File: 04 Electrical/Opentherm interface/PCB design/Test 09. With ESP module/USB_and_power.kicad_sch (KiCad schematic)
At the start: 18 parts, among them J1 USB-C port, U2 SGM2212-3.3XKC3G/TR

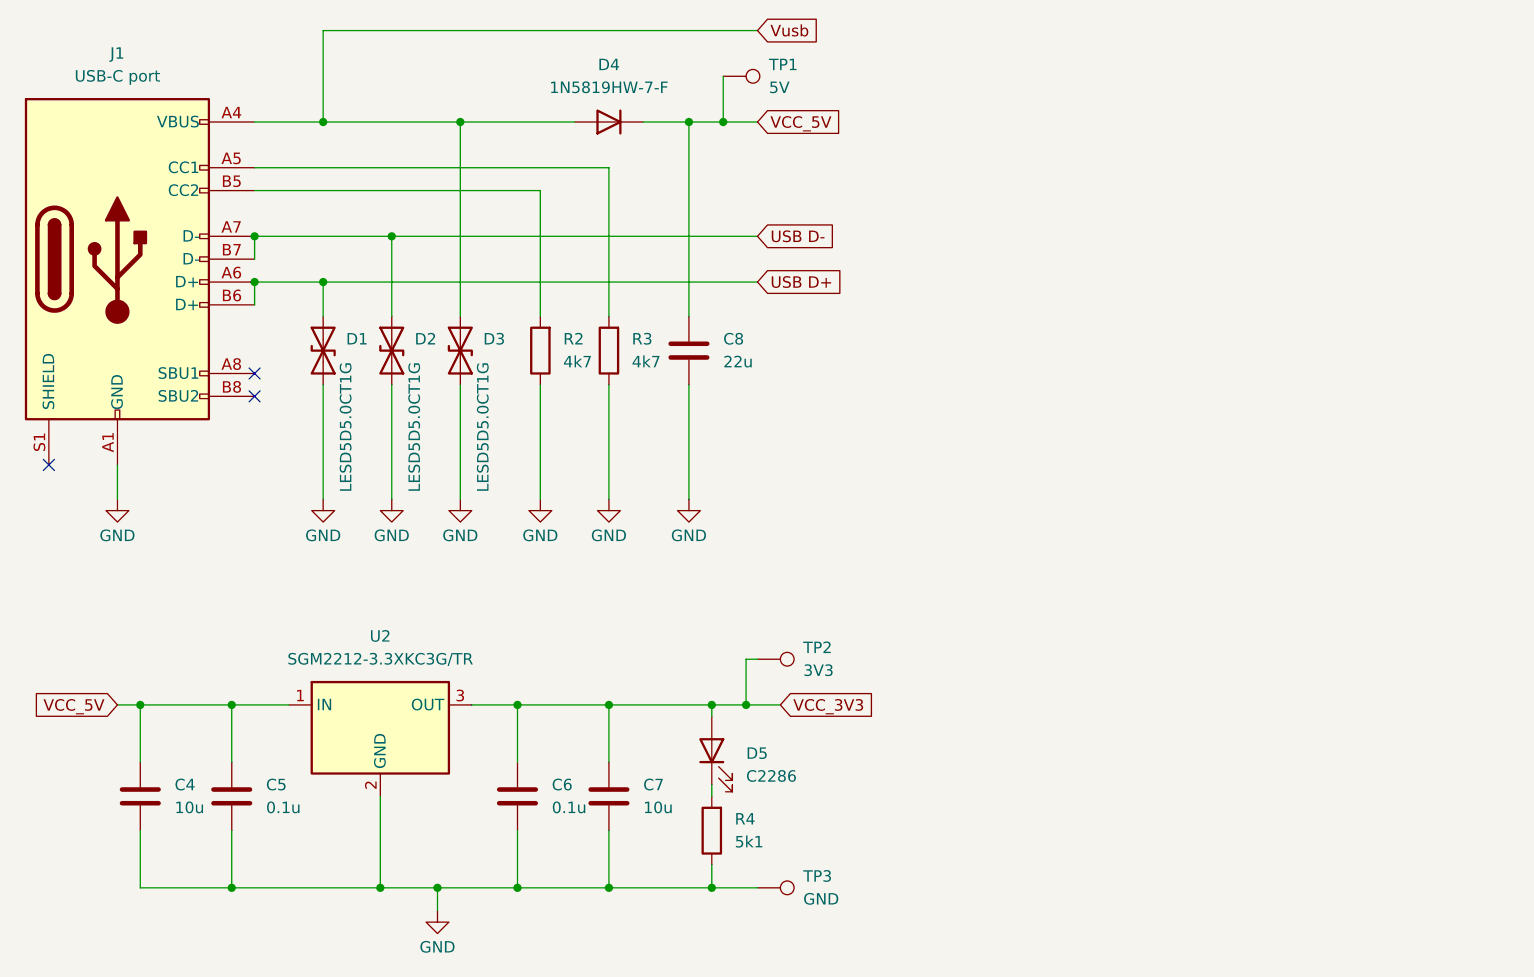
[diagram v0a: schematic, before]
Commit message: Component assignment
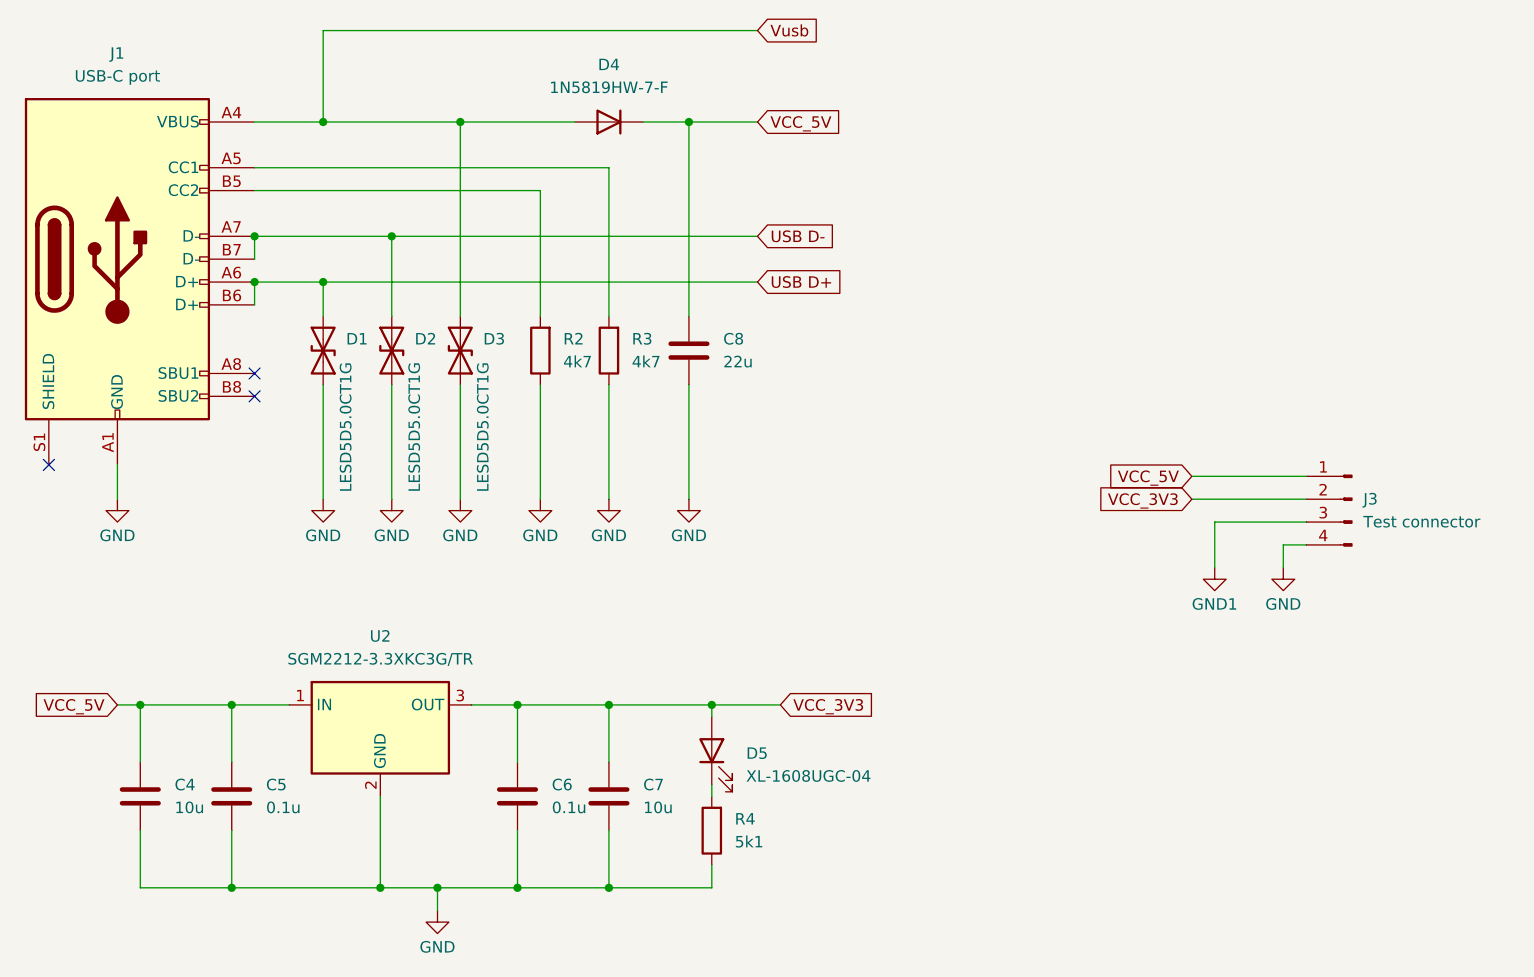
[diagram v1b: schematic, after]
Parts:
- removed TP1: 5V, TestPoint:TestPoint_Pad_D2.5mm, symbol Connector:TestPoint
- removed TP2: 3V3, TestPoint:TestPoint_Pad_D2.5mm, symbol Connector:TestPoint
- removed TP3: GND, TestPoint:TestPoint_Pad_D2.5mm, symbol Connector:TestPoint
- added J3: Test connector, Project:PinHeader_1x04_P2.54mm_Horizontal, symbol Connector:Conn_01x04_Pin
- D5: value C2286 -> XL-1608UGC-04; LCSC Part #  C2286 -> C965804
- R2, R3, R4: footprint Resistor_SMD:R_0201_0603Metric -> Resistor_SMD:R_0603_1608Metric
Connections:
- net GND: now also J3.4 (Pin_4)
- net VCC_3V3: now also J3.2 (Pin_2)
- net VCC_5V: now also J3.1 (Pin_1)
- new net GND1: J3.3 (Pin_3)
